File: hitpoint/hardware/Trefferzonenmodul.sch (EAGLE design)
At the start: 43 parts

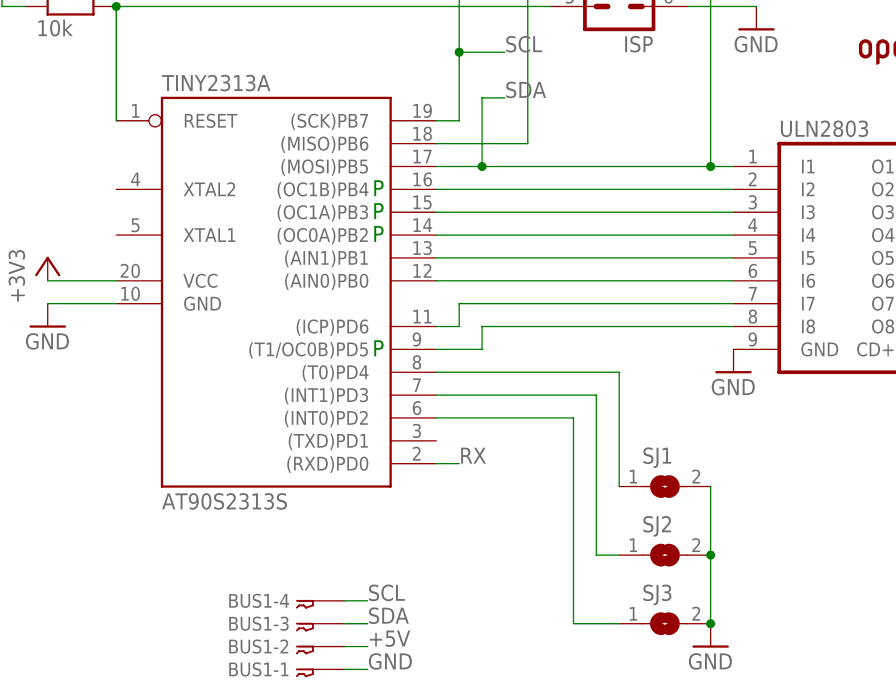
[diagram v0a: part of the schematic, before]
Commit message: hitpoint hardware, touch
hitpoint: sda ist nun nicht mehr mit dem uln verbunden, pegel nun 3,3v
statt 2,5v
touch in x lauffähig
oszi messungen am i2s hinzugefügt
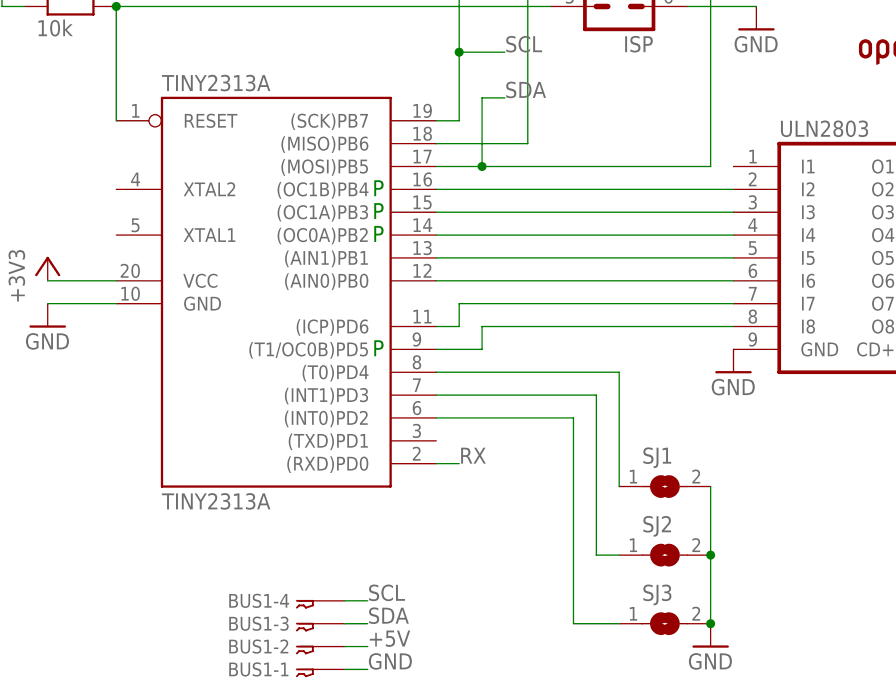
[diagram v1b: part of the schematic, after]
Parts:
- TINY2313A: value AT90S2313S -> TINY2313A; device wz:AT90S2313S -> wz:TINY2313A
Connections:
- net SDA: no longer ULN2803.I1
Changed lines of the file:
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@@
 <grid distance="0.1" unitdist="inch" unit="inch" style="lines" multiple="1" display="no" altdistance="0.01" altunitdist="inch" altunit="inch"/>
 <layers>
-<layer number="1" name="Top" color="4" fill="1" visible="no" active="no"/>
-<layer number="16" name="Bottom" color="1" fill="1" visible="no" active="no"/>
-<layer number="17" name="Pads" color="2" fill="1" visible="no" active="no"/>
-<layer number="18" name="Vias" color="2" fill="1" visible="no" active="no"/>
-<layer number="19" name="Unrouted" color="6" fill="1" visible="no" active="no"/>
-<layer number="20" name="Dimension" color="15" fill="1" visible="no" active="no"/>
-<layer number="21" name="tPlace" color="7" fill="1" visible="no" active="no"/>
-<layer number="22" name="bPlace" color="7" fill="1" visible="no" active="no"/>
-<layer number="23" name="tOrigins" color="15" fill="1" visible="no" active="no"/>
-<layer number="24" name="bOrigins" color="15" fill="1" visible="no" active="no"/>
-<layer number="25" name="tNames" color="7" fill="1" visible="no" active="no"/>
-<layer number="26" name="bNames" color="7" fill="1" visible="no" active="no"/>
-<layer number="27" name="tValues" color="7" fill="1" visible="no" active="no"/>
-<layer number="28" name="bValues" color="7" fill="1" visible="no" active="no"/>
+<layer number="1" name="Top" color="4" fill="1" visible="yes" active="no"/>
+<layer number="16" name="Bottom" color="1" fill="1" visible="yes" active="no"/>
+<layer number="17" name="Pads" color="2" fill="1" visible="yes" active="no"/>
+<layer number="18" name="Vias" color="2" fill="1" visible="yes" active="no"/>
+<layer number="19" name="Unrouted" color="6" fill="1" visible="yes" active="no"/>
+<layer number="20" name="Dimension" color="15" fill="1" visible="yes" active="no"/>
+<layer number="21" name="tPlace" color="7" fill="1" visible="yes" active="no"/>
+<layer number="22" name="bPlace" color="7" fill="1" visible="yes" active="no"/>
+<layer number="23" name="tOrigins" color="15" fill="1" visible="yes" active="no"/>
+<layer number="24" name="bOrigins" color="15" fill="1" visible="yes" active="no"/>
+<layer number="25" name="tNames" color="7" fill="1" visible="yes" active="no"/>
+<layer number="26" name="bNames" color="7" fill="1" visible="yes" active="no"/>
+<layer number="27" name="tValues" color="7" fill="1" visible="yes" active="no"/>
+<layer number="28" name="bValues" color="7" fill="1" visible="yes" active="no"/>
 <layer number="29" name="tStop" color="7" fill="3" visible="no" active="no"/>
 <layer number="30" name="bStop" color="7" fill="6" visible="no" active="no"/>
@@
 <layer number="35" name="tGlue" color="7" fill="4" visible="no" active="no"/>
 <layer number="36" name="bGlue" color="7" fill="5" visible="no" active="no"/>
-<layer number="37" name="tTest" color="7" fill="1" visible="no" active="no"/>
-<layer number="38" name="bTest" color="7" fill="1" visible="no" active="no"/>
+<layer number="37" name="tTest" color="7" fill="1" visible="yes" active="no"/>
+<layer number="38" name="bTest" color="7" fill="1" visible="yes" active="no"/>
 <layer number="39" name="tKeepout" color="4" fill="11" visible="no" active="no"/>
 <layer number="40" name="bKeepout" color="1" fill="11" visible="no" active="no"/>
@@
 <layer number="44" name="Drills" color="7" fill="1" visible="no" active="no"/>
 <layer number="45" name="Holes" color="7" fill="1" visible="no" active="no"/>
-<layer number="46" name="Milling" color="3" fill="1" visible="no" active="no"/>
-<layer number="47" name="Measures" color="7" fill="1" visible="no" active="no"/>
-<layer number="48" name="Document" color="7" fill="1" visible="no" active="no"/>
-<layer number="49" name="Reference" color="7" fill="1" visible="no" active="no"/>
-<layer number="50" name="dxf" color="7" fill="1" visible="no" active="no"/>
-<layer number="51" name="tDocu" color="7" fill="1" visible="no" active="no"/>
-<layer number="52" name="bDocu" color="7" fill="1" visible="no" active="no"/>
-<layer number="53" name="tGND_GNDA" color="7" fill="9" visible="no" active="no"/>
-<layer number="54" name="bGND_GNDA" color="1" fill="9" visible="no" active="no"/>
-<layer number="56" name="wert" color="7" fill="1" visible="no" active="no"/>
-<layer number="57" name="tCAD" color="7" fill="1" visible="no" active="no"/>
+<layer number="46" name="Milling" color="3" fill="1" visible="yes" active="no"/>
+<layer number="47" name="Measures" color="7" fill="1" visible="yes" active="no"/>
+<layer number="48" name="Document" color="7" fill="1" visible="yes" active="no"/>
+<layer number="49" name="Reference" color="7" fill="1" visible="yes" active="no"/>
+<layer number="50" name="dxf" color="7" fill="1" visible="yes" active="no"/>
+<layer number="51" name="tDocu" color="7" fill="1" visible="yes" active="no"/>
+<layer number="52" name="bDocu" color="7" fill="1" visible="yes" active="no"/>
+<layer number="53" name="tGND_GNDA" color="7" fill="9" visible="yes" active="no"/>
+<layer number="54" name="bGND_GNDA" color="1" fill="9" visible="yes" active="no"/>
+<layer number="56" name="wert" color="7" fill="1" visible="yes" active="no"/>
+<layer number="57" name="tCAD" color="7" fill="1" visible="yes" active="no"/>
 <layer number="90" name="Modules" color="5" fill="1" visible="yes" active="yes"/>
 <layer number="91" name="Nets" color="2" fill="1" visible="yes" active="yes"/>
@@
 <layer number="223" name="223bmp" color="24" fill="1" visible="no" active="no"/>
 <layer number="224" name="224bmp" color="25" fill="1" visible="no" active="no"/>
+<layer number="231" name="Eagle3D_PG1" color="7" fill="1" visible="yes" active="yes"/>
+<layer number="232" name="Eagle3D_PG2" color="7" fill="1" visible="yes" active="yes"/>
+<layer number="233" name="Eagle3D_PG3" color="7" fill="1" visible="yes" active="yes"/>
 <layer number="248" name="Housing" color="7" fill="1" visible="yes" active="yes"/>
 <layer number="249" name="Edge" color="7" fill="1" visible="yes" active="yes"/>
@@
 </classes>
 <parts>
-<part name="TINY2313A" library="wz" deviceset="AT90S2313" device="S"/>
+<part name="TINY2313A" library="wz" deviceset="TINY2313A" device=""/>
 <part name="C1" library="wz" deviceset="C-EU" device="C0805" value="100n"/>
 <part name="R1" library="wz" deviceset="R-EU_" device="R0805" value="100"/>
@@
 <wire x1="114.3" y1="83.82" x2="111.76" y2="83.82" width="0.1524" layer="91"/>
 <junction x="88.9" y="63.5"/>
-<pinref part="ULN2803" gate="G$1" pin="I1"/>
-<wire x1="116.84" y1="63.5" x2="114.3" y2="63.5" width="0.1524" layer="91"/>
-<junction x="114.3" y="63.5"/>
-</segment>
-<segment>
+</segment>
+<segment>
